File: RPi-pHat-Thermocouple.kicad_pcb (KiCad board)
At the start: 2 copper layers, 65 x 30 mm, 33 parts, among them J1 RPi_GPIO, P1 CONN_01X02, P2 CONN_01X02, P3 CONN_01X02, P4 CONN_01X02, P6 CONN_01X03, Q1 NUD3124, SW1 Write, U1 MAX31850K, U3 MAX31850K, U4 MAX31850K, U5 AT24CS32, U6 MAX31850K

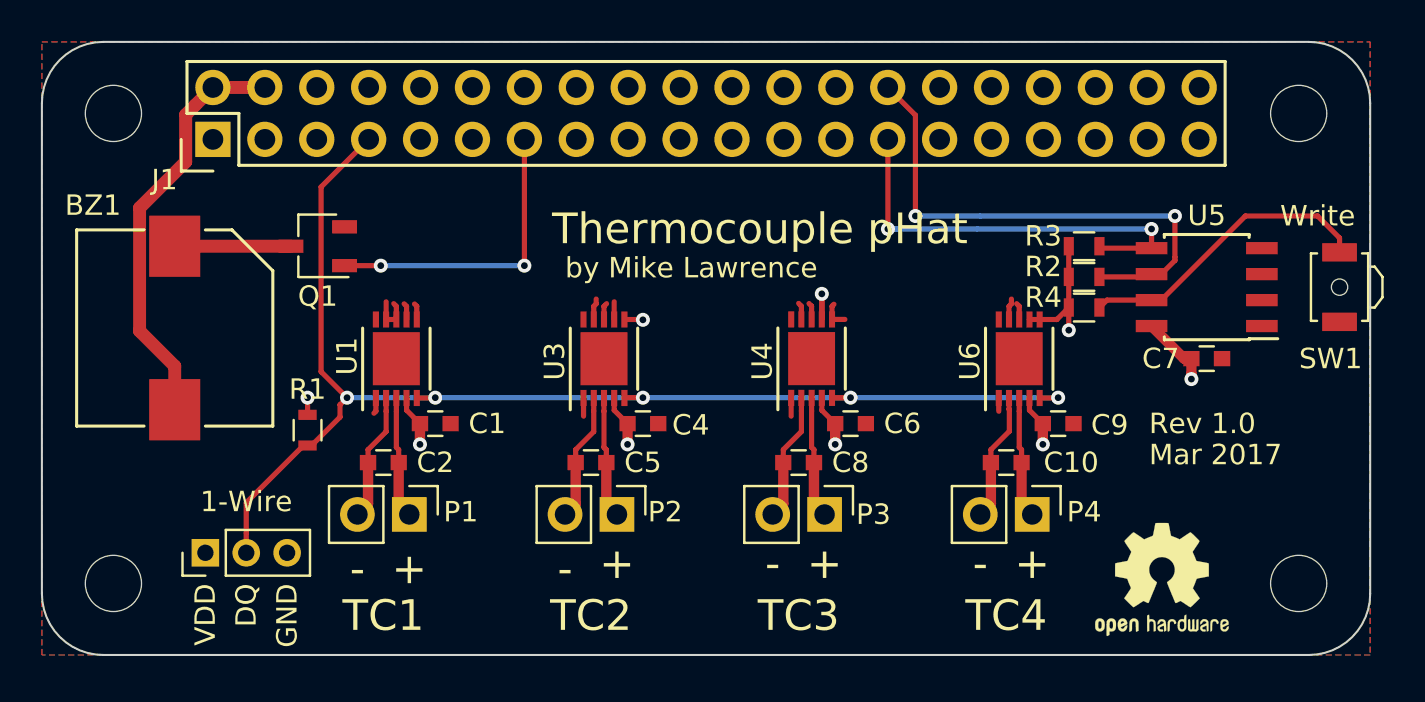
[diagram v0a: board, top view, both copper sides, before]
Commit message: Added U2 and R5
Fixed Alert sounding as soon as power is applied by adding pulldown
(R5). Added Ds18S20 (U2) so the Linux kernel will properly access the
MAX31850K.
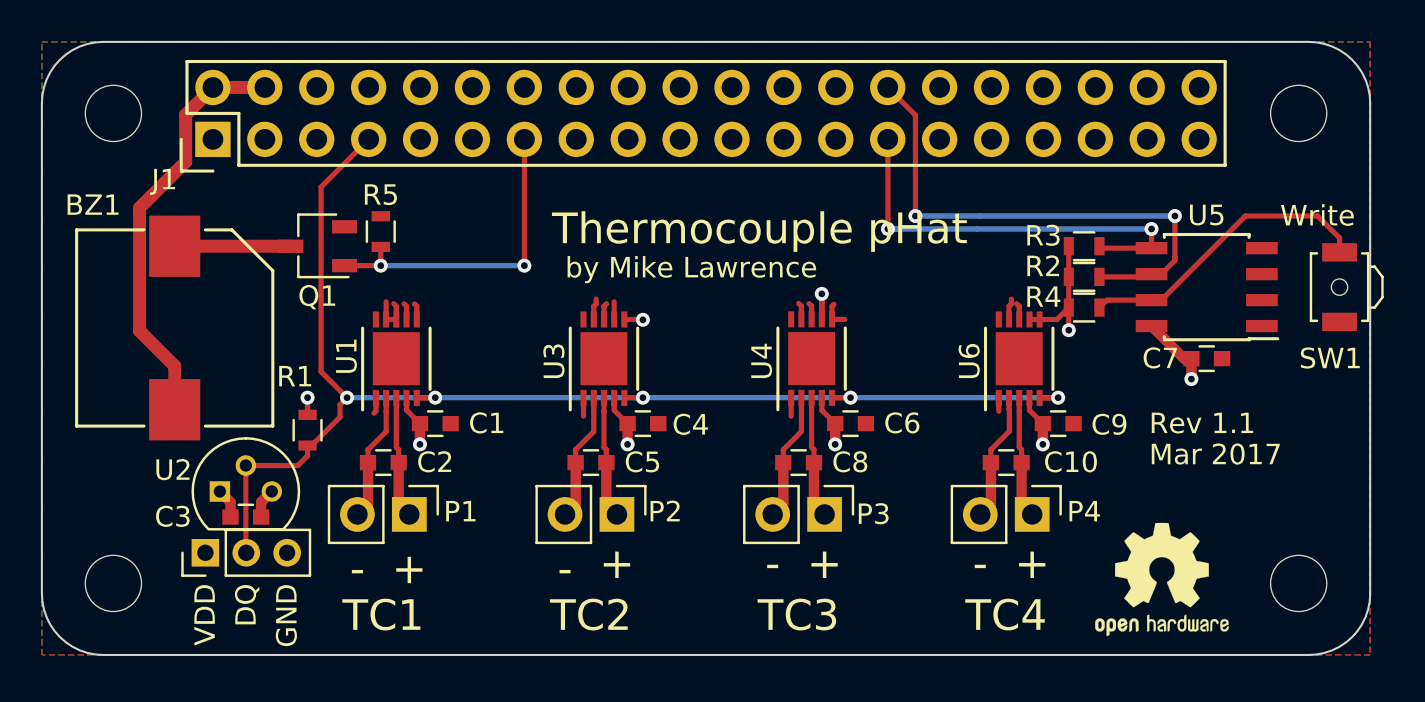
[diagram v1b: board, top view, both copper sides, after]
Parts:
- added C3: 0.1uF, Capacitors_SMD:C_0603, F.Cu at (22.5, 47.8)
- added R5: 4.7k, Resistors_SMD:R_0603, F.Cu at (29.1, 33.8)
- added U2: DS18S20, TO_SOT_Packages_THT:TO-92_Molded_Narrow, F.Cu at (21.2, 46.5)
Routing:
- net +3V3: track 24.2 -> 25.7 mm
- net GND: track 14.7 -> 16.2 mm
- net /W1: track 62.4 -> 63.8 mm
- net /ALERT: track 15.0 -> 15.9 mm
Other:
- board text added: "Rev 1.1"
- board text removed: "1-Wire"
- board text removed: "Rev 1.0"
